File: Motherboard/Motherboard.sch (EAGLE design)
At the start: 10 parts

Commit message: wip
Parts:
- removed J2: (no value), SparkFun-Connectors:CONN_023.5MM
- added AIR_BRAKE: (no value), SparkFun-Connectors:CONN_03
- added POWER_IN: (no value), SparkFun-Connectors:CONN_023.5MM
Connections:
- new net N$3: AIR_BRAKE.2, ARDUINO_NANO1.VIN, POWER_IN.1
- new net N$4: AIR_BRAKE.3, ARDUINO_NANO1.D6
- net GND: now also AIR_BRAKE.1, POWER_IN.2
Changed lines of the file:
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@@
 <?xml version="1.0" encoding="utf-8"?>
 <!DOCTYPE eagle SYSTEM "eagle.dtd">
-<eagle version="9.3.0">
+<eagle version="9.3.1">
 <drawing>
 <settings>
@@
 <part name="ALTIMETER2" library="microbuilder" deviceset="HEADER-1X5" device="70MIL"/>
 <part name="J1" library="SparkFun-Connectors" deviceset="CONN_08X2" device="_HEADER"/>
-<part name="J2" library="SparkFun-Connectors" deviceset="CONN_02" device="3.5MM"/>
+<part name="POWER_IN" library="SparkFun-Connectors" deviceset="CONN_02" device="3.5MM"/>
+<part name="AIR_BRAKE" library="SparkFun-Connectors" deviceset="CONN_03" device=""/>
 </parts>
 <sheets>
@@
 <attribute name="NAME" x="-39.37" y="91.948" size="1.778" layer="95" font="vector"/>
 </instance>
-<instance part="J2" gate="G$1" x="2.54" y="76.2" smashed="yes">
-<attribute name="VALUE" x="0" y="71.374" size="1.778" layer="96" font="vector"/>
-<attribute name="NAME" x="0" y="81.788" size="1.778" layer="95" font="vector"/>
+<instance part="POWER_IN" gate="G$1" x="-30.48" y="15.24" smashed="yes">
+<attribute name="VALUE" x="-33.02" y="10.414" size="1.778" layer="96" font="vector"/>
+<attribute name="NAME" x="-33.02" y="20.828" size="1.778" layer="95" font="vector"/>
+</instance>
+<instance part="AIR_BRAKE" gate="J$1" x="-83.82" y="15.24" smashed="yes">
+<attribute name="VALUE" x="-86.36" y="7.874" size="1.778" layer="96" font="vector"/>
+<attribute name="NAME" x="-86.36" y="20.828" size="1.778" layer="95" font="vector"/>
 </instance>
 </instances>
@@
 <segment>
 <pinref part="ARDUINO_NANO1" gate="G$1" pin="GND@2"/>
-<wire x1="-21.59" y1="5.08" x2="7.62" y2="5.08" width="0.1524" layer="91"/>
+<wire x1="-21.59" y1="5.08" x2="-15.24" y2="5.08" width="0.1524" layer="91"/>
 <label x="-20.32" y="5.08" size="1.778" layer="95"/>
 <pinref part="IMU" gate="G$1" pin="GND"/>
+<wire x1="-15.24" y1="5.08" x2="7.62" y2="5.08" width="0.1524" layer="91"/>
 <wire x1="7.62" y1="5.08" x2="7.62" y2="-11.43" width="0.1524" layer="91"/>
 <wire x1="7.62" y1="-11.43" x2="17.78" y2="-11.43" width="0.1524" layer="91"/>
@@
 <wire x1="7.62" y1="5.08" x2="7.62" y2="43.18" width="0.1524" layer="91"/>
 <wire x1="7.62" y1="43.18" x2="22.86" y2="43.18" width="0.1524" layer="91"/>
+<pinref part="POWER_IN" gate="G$1" pin="2"/>
+<wire x1="-22.86" y1="17.78" x2="-15.24" y2="17.78" width="0.1524" layer="91"/>
+<wire x1="-15.24" y1="17.78" x2="-15.24" y2="5.08" width="0.1524" layer="91"/>
+<junction x="-15.24" y="5.08"/>
+<pinref part="AIR_BRAKE" gate="J$1" pin="1"/>
+<wire x1="-76.2" y1="12.7" x2="-35.56" y2="12.7" width="0.1524" layer="91"/>
+<wire x1="-35.56" y1="12.7" x2="-35.56" y2="22.86" width="0.1524" layer="91"/>
+<wire x1="-35.56" y1="22.86" x2="-15.24" y2="22.86" width="0.1524" layer="91"/>
+<wire x1="-15.24" y1="22.86" x2="-15.24" y2="17.78" width="0.1524" layer="91"/>
+<junction x="-15.24" y="17.78"/>
 </segment>
 </net>
@@
 </segment>
 </net>
+<net name="N$3" class="0">
+<segment>
+<pinref part="AIR_BRAKE" gate="J$1" pin="2"/>
+<wire x1="-76.2" y1="15.24" x2="-38.1" y2="15.24" width="0.1524" layer="91"/>
+<wire x1="-38.1" y1="15.24" x2="-38.1" y2="25.4" width="0.1524" layer="91"/>
+<wire x1="-38.1" y1="25.4" x2="-17.78" y2="25.4" width="0.1524" layer="91"/>
+<wire x1="-17.78" y1="25.4" x2="-17.78" y2="15.24" width="0.1524" layer="91"/>
+<pinref part="POWER_IN" gate="G$1" pin="1"/>
+<pinref part="ARDUINO_NANO1" gate="G$1" pin="VIN"/>
+<wire x1="-22.86" y1="15.24" x2="-21.59" y2="15.24" width="0.1524" layer="91"/>
+<wire x1="-21.59" y1="15.24" x2="-21.59" y2="7.62" width="0.1524" layer="91"/>
+<wire x1="-17.78" y1="15.24" x2="-22.86" y2="15.24" width="0.1524" layer="91"/>
+<junction x="-22.86" y="15.24"/>
+</segment>
+</net>
+<net name="N$4" class="0">
+<segment>
+<pinref part="AIR_BRAKE" gate="J$1" pin="3"/>
+<wire x1="-76.2" y1="17.78" x2="-71.12" y2="17.78" width="0.1524" layer="91"/>
+<wire x1="-71.12" y1="17.78" x2="-71.12" y2="-12.7" width="0.1524" layer="91"/>
+<pinref part="ARDUINO_NANO1" gate="G$1" pin="D6"/>
+<wire x1="-71.12" y1="-12.7" x2="-62.23" y2="-12.7" width="0.1524" layer="91"/>
+</segment>
+</net>

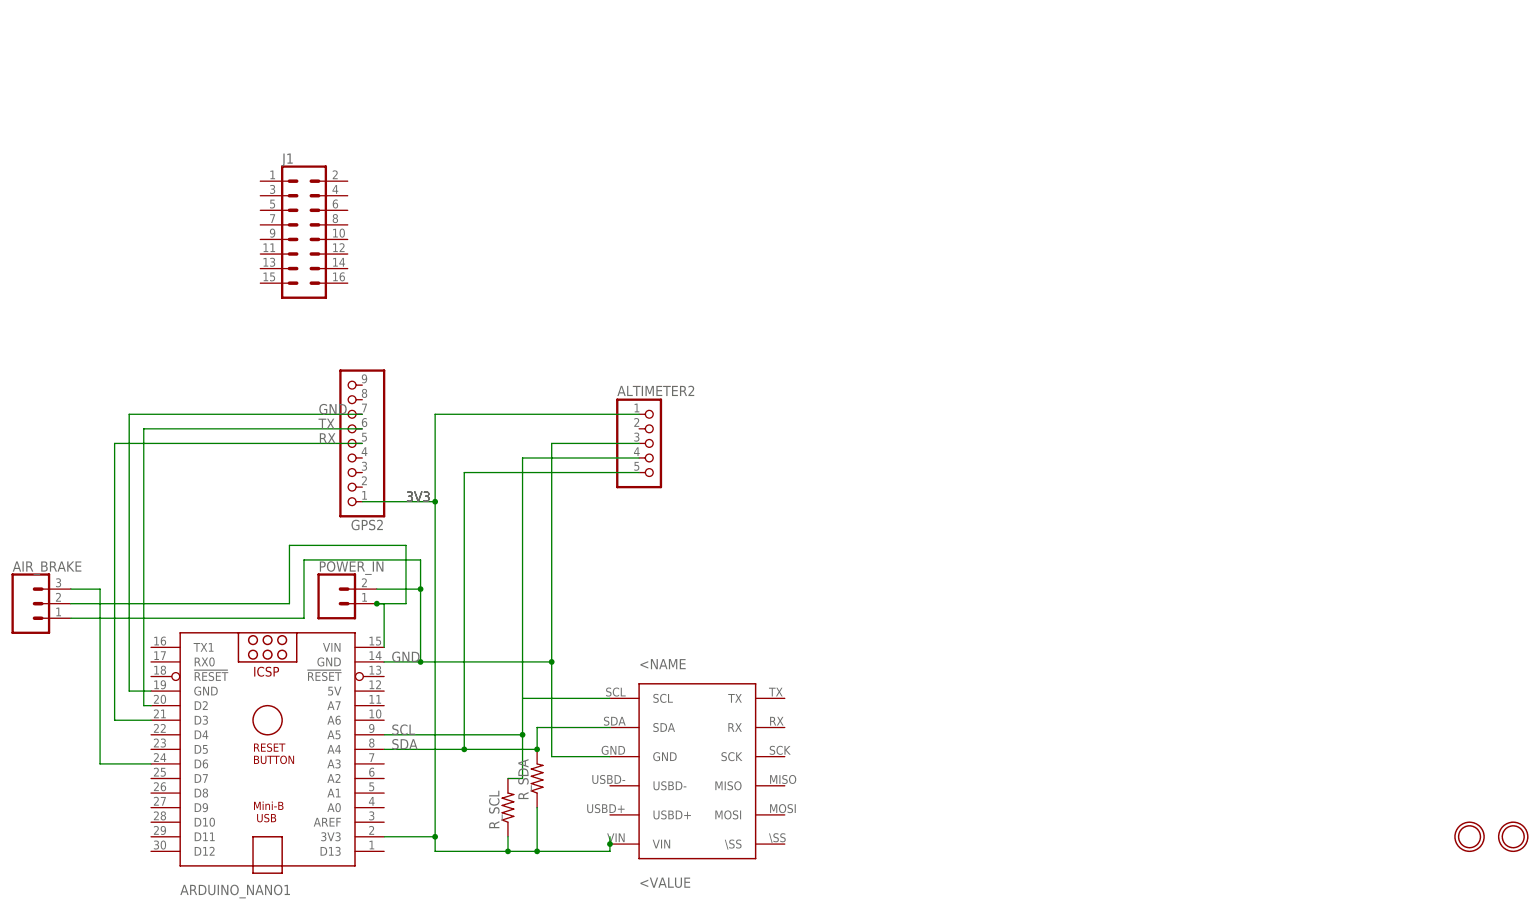
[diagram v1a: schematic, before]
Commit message: add SD card, wire radio
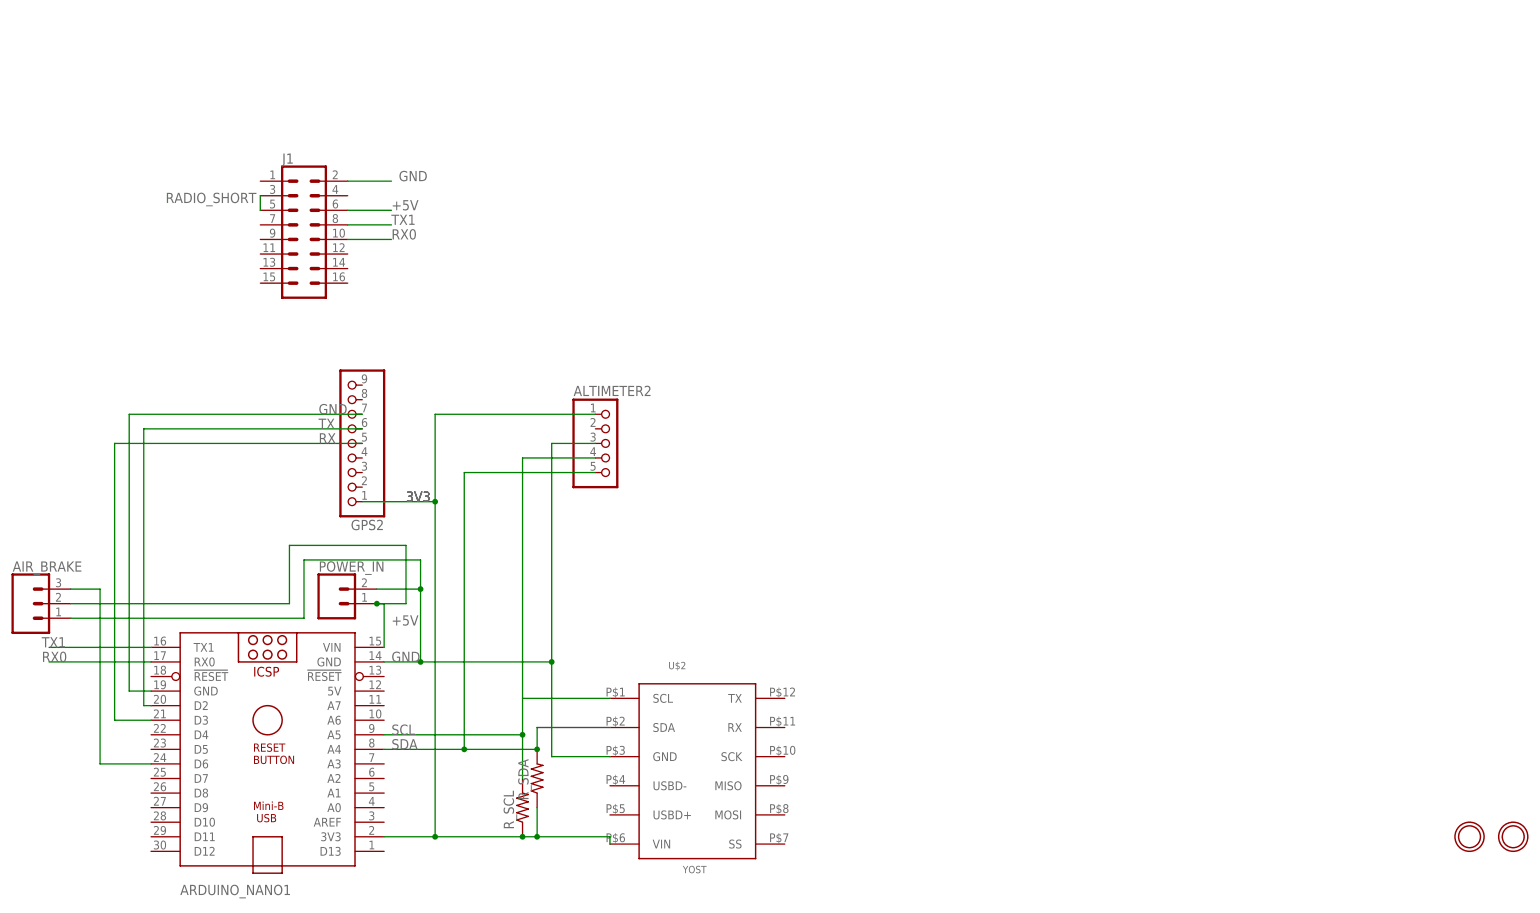
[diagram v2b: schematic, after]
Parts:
- removed IMU: YOSTLABSIMU, YOST LABS IMU:YOSTLABSIMU
- added U$2: YOST, ArduinoNanoV30:YOST
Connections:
- removed net N$3: AIR_BRAKE.2, ARDUINO_NANO1.VIN, POWER_IN.1
- new net +5V: AIR_BRAKE.2, ARDUINO_NANO1.VIN, J1.6, POWER_IN.1
- new net RADIO_SHORT: J1.3, J1.5
- new net RX0: ARDUINO_NANO1.RX0, J1.10
- new net TX1: ARDUINO_NANO1.TX1, J1.8
- net 3V3: now also U$2.VIN; no longer IMU.VIN
- net GND: now also J1.2, U$2.GND; no longer IMU.GND
- net SCL: now also U$2.SCL; no longer IMU.SCL
- net SDA: now also U$2.SDA; no longer IMU.SDA
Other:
- moved on the sheet: ALTIMETER2, R_SCL
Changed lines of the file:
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@@
 <setting verticaltext="up"/>
 </settings>
-<grid distance="0.1" unitdist="inch" unit="inch" style="lines" multiple="1" display="no" altdistance="0.01" altunitdist="inch" altunit="inch"/>
+<grid distance="0.05" unitdist="inch" unit="inch" style="lines" multiple="1" display="no" altdistance="0.01" altunitdist="inch" altunit="inch"/>
 <layers>
 <layer number="1" name="Top" color="4" fill="1" visible="no" active="no"/>
@@
 <parts>
 <part name="ARDUINO_NANO1" library="ArduinoNanoV30" deviceset="ARDUINO_NANO" device=""/>
-<part name="IMU" library="YOST LABS IMU" deviceset="YOSTLABSIMU" device=""/>
 <part name="R_SCL" library="rcl" library_urn="urn:adsk.eagle:library:334" deviceset="R-US_" device="R0603" package3d_urn="urn:adsk.eagle:package:23555/3"/>
 <part name="R_SDA" library="rcl" library_urn="urn:adsk.eagle:library:334" deviceset="R-US_" device="R0603" package3d_urn="urn:adsk.eagle:package:23555/3"/>
@@
 <part name="POWER_IN" library="SparkFun-Connectors" deviceset="CONN_02" device="3.5MM"/>
 <part name="AIR_BRAKE" library="SparkFun-Connectors" deviceset="CONN_03" device=""/>
+<part name="U$2" library="ArduinoNanoV30" deviceset="YOST" device=""/>
 </parts>
 <sheets>
@@
 <attribute name="VALUE" x="-57.15" y="-38.1" size="1.778" layer="96"/>
 </instance>
-<instance part="IMU" gate="G$1" x="147.32" y="-19.05" smashed="yes"/>
-<instance part="R_SCL" gate="G$1" x="0" y="-20.32" smashed="yes" rot="R90">
-<attribute name="NAME" x="-1.4986" y="-24.13" size="1.778" layer="95" rot="R90"/>
-<attribute name="VALUE" x="3.302" y="-24.13" size="1.778" layer="96" rot="R90"/>
+<instance part="R_SCL" gate="G$1" x="2.54" y="-20.32" smashed="yes" rot="R90">
+<attribute name="NAME" x="1.0414" y="-24.13" size="1.778" layer="95" rot="R90"/>
+<attribute name="VALUE" x="5.842" y="-24.13" size="1.778" layer="96" rot="R90"/>
 </instance>
 <instance part="R_SDA" gate="G$1" x="5.08" y="-15.24" smashed="yes" rot="R90">
@@
 <attribute name="VALUE" x="-21.59" y="58.42" size="1.778" layer="96" rot="R180"/>
 </instance>
-<instance part="ALTIMETER2" gate="A" x="25.4" y="43.18" smashed="yes">
-<attribute name="NAME" x="19.05" y="51.435" size="1.778" layer="95"/>
-<attribute name="VALUE" x="19.05" y="33.02" size="1.778" layer="96"/>
+<instance part="ALTIMETER2" gate="A" x="17.78" y="43.18" smashed="yes">
+<attribute name="NAME" x="11.43" y="51.435" size="1.778" layer="95"/>
+<attribute name="VALUE" x="11.43" y="33.02" size="1.778" layer="96"/>
 </instance>
 <instance part="J1" gate="J1" x="-35.56" y="78.74" smashed="yes">
@@
 <attribute name="VALUE" x="-86.36" y="7.874" size="1.778" layer="96" font="vector"/>
 <attribute name="NAME" x="-86.36" y="20.828" size="1.778" layer="95" font="vector"/>
+</instance>
+<instance part="U$2" gate="G$1" x="33.02" y="-11.43" smashed="yes">
+<attribute name="NAME" x="27.94" y="3.81" size="1.27" layer="95"/>
+<attribute name="VALUE" x="30.48" y="-31.75" size="1.27" layer="96"/>
 </instance>
 </instances>
@@
 <label x="-17.78" y="33.02" size="1.778" layer="95"/>
 <label x="-17.78" y="33.02" size="1.778" layer="95"/>
-<wire x1="-12.7" y1="-25.4" x2="-12.7" y2="-27.94" width="0.1524" layer="91"/>
 <junction x="-12.7" y="-25.4"/>
-<pinref part="IMU" gate="G$1" pin="VIN"/>
+<wire x1="-12.7" y1="-25.4" x2="2.54" y2="-25.4" width="0.1524" layer="91"/>
+<wire x1="2.54" y1="-25.4" x2="5.08" y2="-25.4" width="0.1524" layer="91"/>
+<wire x1="5.08" y1="-25.4" x2="17.78" y2="-25.4" width="0.1524" layer="91"/>
 <wire x1="17.78" y1="-25.4" x2="17.78" y2="-26.67" width="0.1524" layer="91"/>
-<wire x1="-12.7" y1="-27.94" x2="0" y2="-27.94" width="0.1524" layer="91"/>
-<wire x1="0" y1="-27.94" x2="5.08" y2="-27.94" width="0.1524" layer="91"/>
-<wire x1="5.08" y1="-27.94" x2="17.78" y2="-27.94" width="0.1524" layer="91"/>
-<wire x1="17.78" y1="-27.94" x2="17.78" y2="-26.67" width="0.1524" layer="91"/>
-<junction x="17.78" y="-26.67"/>
 <pinref part="R_SCL" gate="G$1" pin="1"/>
-<wire x1="0" y1="-25.4" x2="0" y2="-27.94" width="0.1524" layer="91"/>
-<junction x="0" y="-27.94"/>
+<junction x="2.54" y="-25.4"/>
 <pinref part="R_SDA" gate="G$1" pin="1"/>
-<wire x1="5.08" y1="-20.32" x2="5.08" y2="-27.94" width="0.1524" layer="91"/>
-<junction x="5.08" y="-27.94"/>
+<wire x1="5.08" y1="-20.32" x2="5.08" y2="-25.4" width="0.1524" layer="91"/>
+<junction x="5.08" y="-25.4"/>
 <pinref part="GPS2" gate="A" pin="1"/>
 <wire x1="-12.7" y1="33.02" x2="-12.7" y2="48.26" width="0.1524" layer="91"/>
 <junction x="-12.7" y="33.02"/>
 <pinref part="ALTIMETER2" gate="A" pin="1"/>
-<wire x1="-12.7" y1="48.26" x2="22.86" y2="48.26" width="0.1524" layer="91"/>
+<wire x1="-12.7" y1="48.26" x2="15.24" y2="48.26" width="0.1524" layer="91"/>
+<pinref part="U$2" gate="G$1" pin="VIN"/>
 </segment>
 </net>
@@
 <wire x1="-21.59" y1="5.08" x2="-15.24" y2="5.08" width="0.1524" layer="91"/>
 <label x="-20.32" y="5.08" size="1.778" layer="95"/>
-<pinref part="IMU" gate="G$1" pin="GND"/>
 <wire x1="-15.24" y1="5.08" x2="7.62" y2="5.08" width="0.1524" layer="91"/>
 <wire x1="7.62" y1="5.08" x2="7.62" y2="-11.43" width="0.1524" layer="91"/>
@@
 <pinref part="ALTIMETER2" gate="A" pin="3"/>
 <wire x1="7.62" y1="5.08" x2="7.62" y2="43.18" width="0.1524" layer="91"/>
-<wire x1="7.62" y1="43.18" x2="22.86" y2="43.18" width="0.1524" layer="91"/>
+<wire x1="7.62" y1="43.18" x2="15.24" y2="43.18" width="0.1524" layer="91"/>
 <pinref part="POWER_IN" gate="G$1" pin="2"/>
 <wire x1="-22.86" y1="17.78" x2="-15.24" y2="17.78" width="0.1524" layer="91"/>
@@
 <wire x1="-15.24" y1="22.86" x2="-15.24" y2="17.78" width="0.1524" layer="91"/>
 <junction x="-15.24" y="17.78"/>
+<pinref part="U$2" gate="G$1" pin="GND"/>
+</segment>
+<segment>
+<pinref part="J1" gate="J1" pin="2"/>
+<wire x1="-27.94" y1="88.9" x2="-20.32" y2="88.9" width="0.1524" layer="91"/>
+<label x="-19.05" y="88.9" size="1.778" layer="95"/>
 </segment>
 </net>
@@
 <wire x1="-7.62" y1="-10.16" x2="-21.59" y2="-10.16" width="0.1524" layer="91"/>
 <label x="-20.32" y="-10.16" size="1.778" layer="95"/>
-<pinref part="IMU" gate="G$1" pin="SDA"/>
 <wire x1="17.78" y1="-6.35" x2="5.08" y2="-6.35" width="0.1524" layer="91"/>
 <wire x1="5.08" y1="-6.35" x2="5.08" y2="-10.16" width="0.1524" layer="91"/>
@@
 <junction x="5.08" y="-10.16"/>
 <pinref part="ALTIMETER2" gate="A" pin="5"/>
-<wire x1="-7.62" y1="38.1" x2="22.86" y2="38.1" width="0.1524" layer="91"/>
+<wire x1="-7.62" y1="38.1" x2="15.24" y2="38.1" width="0.1524" layer="91"/>
+<pinref part="U$2" gate="G$1" pin="SDA"/>
 </segment>
 </net>
@@
 <wire x1="2.54" y1="-1.27" x2="2.54" y2="40.64" width="0.1524" layer="91"/>
 <label x="-20.32" y="-7.62" size="1.778" layer="95"/>
-<pinref part="IMU" gate="G$1" pin="SCL"/>
 <wire x1="17.78" y1="-1.27" x2="2.54" y2="-1.27" width="0.1524" layer="91"/>
 <pinref part="R_SCL" gate="G$1" pin="2"/>
-<wire x1="0" y1="-15.24" x2="2.54" y2="-15.24" width="0.1524" layer="91"/>
 <wire x1="2.54" y1="-15.24" x2="2.54" y2="-7.62" width="0.1524" layer="91"/>
 <junction x="2.54" y="-7.62"/>
 <pinref part="ALTIMETER2" gate="A" pin="4"/>
-<wire x1="2.54" y1="40.64" x2="22.86" y2="40.64" width="0.1524" layer="91"/>
-</segment>
-</net>
-<net name="N$3" class="0">
+<wire x1="2.54" y1="40.64" x2="15.24" y2="40.64" width="0.1524" layer="91"/>
+<pinref part="U$2" gate="G$1" pin="SCL"/>
+</segment>
+</net>
+<net name="+5V" class="0">
 <segment>
 <pinref part="AIR_BRAKE" gate="J$1" pin="2"/>
@@
 <wire x1="-17.78" y1="15.24" x2="-22.86" y2="15.24" width="0.1524" layer="91"/>
 <junction x="-22.86" y="15.24"/>
+<label x="-20.32" y="11.43" size="1.778" layer="95"/>
+</segment>
+<segment>
+<pinref part="J1" gate="J1" pin="6"/>
+<wire x1="-27.94" y1="83.82" x2="-20.32" y2="83.82" width="0.1524" layer="91"/>
+<label x="-20.32" y="83.82" size="1.778" layer="95"/>
 </segment>
 </net>
@@
 </segment>
 </net>
+<net name="RADIO_SHORT" class="0">
+<segment>
+<pinref part="J1" gate="J1" pin="3"/>
+<pinref part="J1" gate="J1" pin="5"/>
+<wire x1="-43.18" y1="86.36" x2="-43.18" y2="83.82" width="0.1524" layer="91"/>
+<label x="-59.69" y="85.09" size="1.778" layer="95"/>
+</segment>
+</net>
+<net name="TX1" class="0">
+<segment>
+<pinref part="J1" gate="J1" pin="8"/>
+<wire x1="-27.94" y1="81.28" x2="-20.32" y2="81.28" width="0.1524" layer="91"/>
+<label x="-20.32" y="81.28" size="1.778" layer="95"/>
+</segment>
+<segment>
+<pinref part="ARDUINO_NANO1" gate="G$1" pin="TX1"/>
+<wire x1="-62.23" y1="7.62" x2="-80.01" y2="7.62" width="0.1524" layer="91"/>
+<label x="-81.28" y="7.62" size="1.778" layer="95"/>
+</segment>
+</net>
+<net name="RX0" class="0">
+<segment>
+<pinref part="J1" gate="J1" pin="10"/>
+<wire x1="-27.94" y1="78.74" x2="-20.32" y2="78.74" width="0.1524" layer="91"/>
+<label x="-20.32" y="78.74" size="1.778" layer="95"/>
+</segment>
+<segment>
+<pinref part="ARDUINO_NANO1" gate="G$1" pin="RX0"/>
+<wire x1="-62.23" y1="5.08" x2="-80.01" y2="5.08" width="0.1524" layer="91"/>
+<label x="-81.28" y="5.08" size="1.778" layer="95"/>
+</segment>
+</net>

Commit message: library updates
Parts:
- added U$5: DFR0229, uORocketry-parts:DFR0229
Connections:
- new net 5V: ARDUINO_NANO1.5V, U$5.5V
- net GND: now also U$5.GND
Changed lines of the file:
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@@
 <part name="AIR_BRAKE" library="SparkFun-Connectors" deviceset="CONN_03" device=""/>
 <part name="U$2" library="ArduinoNanoV30" deviceset="YOST" device=""/>
+<part name="U$5" library="uORocketry-parts" deviceset="DFR0229" device=""/>
 </parts>
 <sheets>
@@
 <attribute name="NAME" x="27.94" y="3.81" size="1.27" layer="95"/>
 <attribute name="VALUE" x="30.48" y="-31.75" size="1.27" layer="96"/>
+</instance>
+<instance part="U$5" gate="G$1" x="58.42" y="33.02" smashed="yes" rot="R180">
+<attribute name="NAME" x="63.5" y="23.876" size="1.778" layer="95" rot="R180"/>
+<attribute name="VALUE" x="63.5" y="44.45" size="1.778" layer="96" rot="R180"/>
 </instance>
 </instances>
@@
 <label x="-19.05" y="88.9" size="1.778" layer="95"/>
 </segment>
+<segment>
+<pinref part="U$5" gate="G$1" pin="GND"/>
+<wire x1="48.26" y1="36.83" x2="40.64" y2="36.83" width="0.1524" layer="91"/>
+<label x="40.64" y="36.83" size="1.778" layer="95"/>
+</segment>
 </net>
 <net name="SDA" class="0">
@@
 </segment>
 </net>
+<net name="5V" class="0">
+<segment>
+<pinref part="ARDUINO_NANO1" gate="G$1" pin="5V"/>
+<wire x1="-21.59" y1="0" x2="-19.05" y2="0" width="0.1524" layer="91"/>
+<label x="-17.78" y="0" size="1.778" layer="95"/>
+</segment>
+<segment>
+<pinref part="U$5" gate="G$1" pin="5V"/>
+<wire x1="48.26" y1="39.37" x2="40.64" y2="39.37" width="0.1524" layer="91"/>
+<label x="41.91" y="40.64" size="1.778" layer="95"/>
+</segment>
+</net>
